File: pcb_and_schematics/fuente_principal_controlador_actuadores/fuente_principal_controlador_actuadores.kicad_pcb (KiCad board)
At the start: 2 copper layers, 166.1 x 108.2 mm, 78 parts, among them J1 Screw_Terminal_01x02, J10 Screw_Terminal_01x02, J11 Conn_01x15_Female, J12 Conn_01x15_Female, J2 Screw_Terminal_01x02, J3 Screw_Terminal_01x02, J4 Screw_Terminal_01x02, J5 Screw_Terminal_01x02, J6 Screw_Terminal_01x02, J7 Screw_Terminal_01x02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

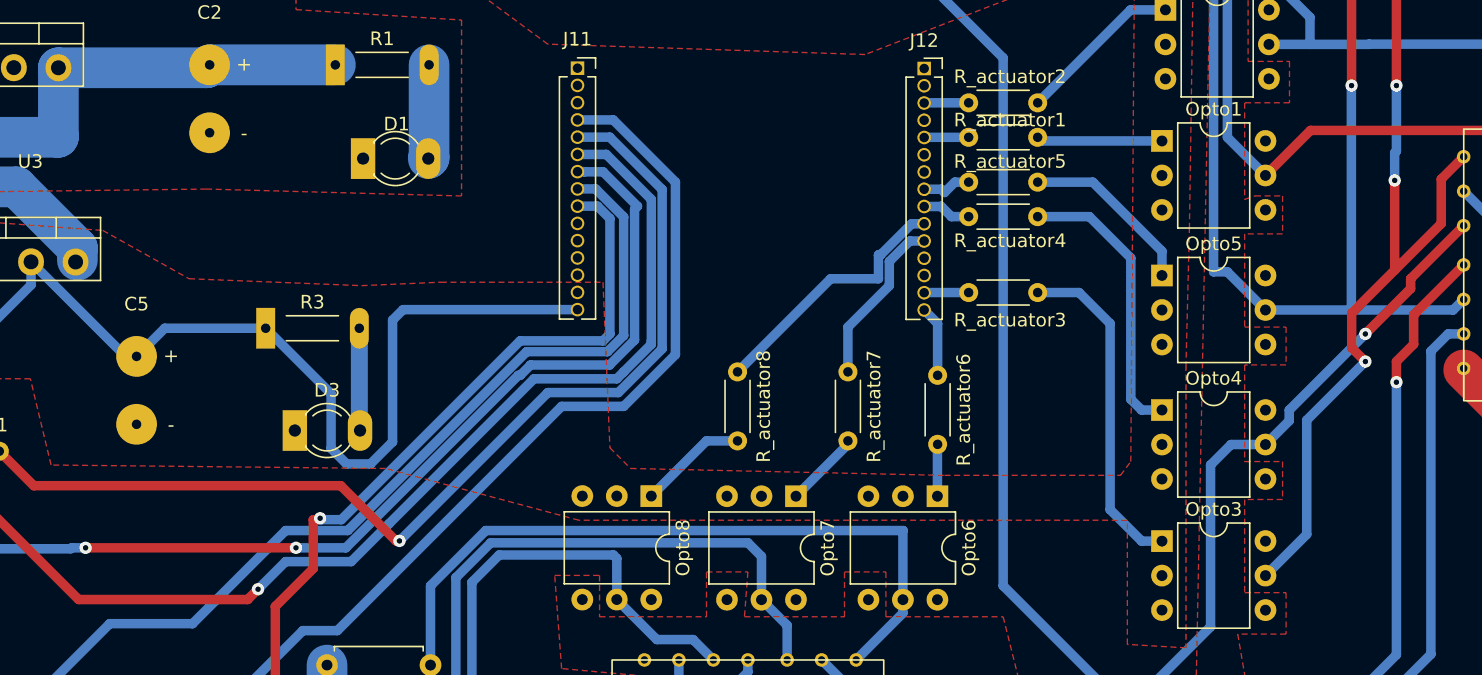
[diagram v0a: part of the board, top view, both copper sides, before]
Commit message: updated size of vias true holes, to make them bigger
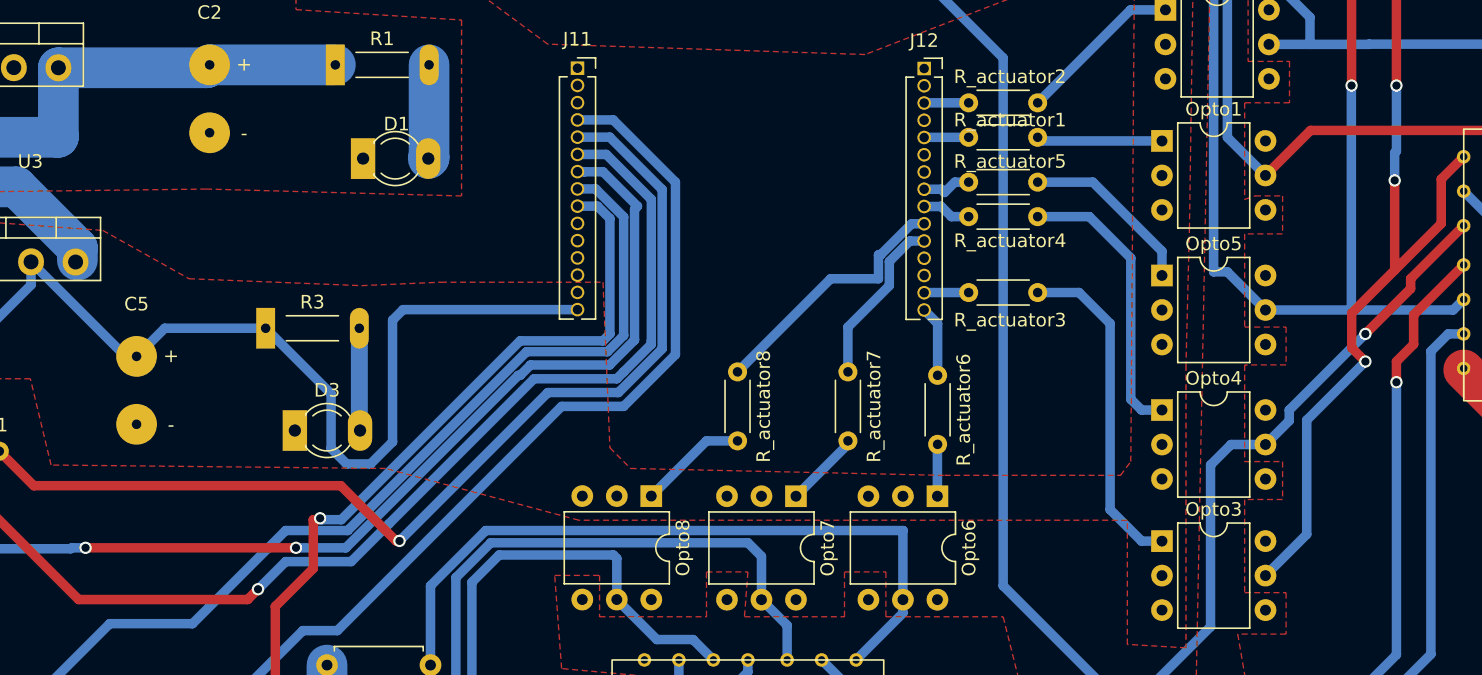
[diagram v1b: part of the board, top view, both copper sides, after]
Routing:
- net GND 3.3V: track 0.65 -> 0.00 mm
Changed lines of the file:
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@@
     (pts (xy 202.438 25.4) (xy 202.692 133.604))
     (height -7.844)
-    (gr_text "108,2043 mm" (at 212.208973 79.479362 270.1344969) (layer "F.Cu")
+    (gr_text "108.2043 mm" (at 212.208973 79.479362 270.1344969) (layer "F.Cu")
       (effects (font (size 1.5 1.5) (thickness 0.3)))
     )
@@
     (pts (xy 35.306 134.874) (xy 200.406 134.874))
     (height 4.040198)
-    (gr_text "165,1000 mm" (at 123.698 142.24) (layer "F.Cu")
+    (gr_text "165.1000 mm" (at 123.698 142.24) (layer "F.Cu")
       (effects (font (size 1.5 1.5) (thickness 0.3)))
     )
@@
   (segment (start 57.595 64.932) (end 62.489 60.038) (width 3) (layer "B.Cu") (net 2))
   (segment (start 62.489 60.038) (end 69.067098 60.038) (width 3) (layer "B.Cu") (net 2))
-  (segment (start 78.382 77.978) (end 77.924 77.52) (width 0.7) (layer "B.Cu") (net 3))
   (segment (start 92.245674 75.265674) (end 92.245674 79.291674) (width 0.7) (layer "B.Cu") (net 4))
   (segment (start 79.996 70.448) (end 77.924 72.52) (width 0.7) (layer "B.Cu") (net 4))
@@
   (segment (start 73.66 90.424) (end 62.738 79.502) (width 0.7) (layer "F.Cu") (net 19))
   (segment (start 86.106 90.424) (end 73.66 90.424) (width 0.7) (layer "F.Cu") (net 19))
-  (via (at 86.868 89.662) (size 0.91) (drill 0.4) (layers "F.Cu" "B.Cu") (net 19))
+  (via (at 86.868 89.662) (size 0.91) (drill 0.6) (layers "F.Cu" "B.Cu") (net 19))
   (segment (start 93.726 87.63) (end 88.9 87.63) (width 0.7) (layer "B.Cu") (net 19))
   (segment (start 110.39 57.648) (end 112.512 57.648) (width 0.7) (layer "B.Cu") (net 19))
@@
   (segment (start 112.512 57.648) (end 115.824 60.96) (width 0.7) (layer "B.Cu") (net 19))
   (segment (start 89.662 86.614) (end 74.168 86.614) (width 0.7) (layer "F.Cu") (net 20))
-  (via (at 89.662 86.614) (size 0.91) (drill 0.4) (layers "F.Cu" "B.Cu") (free) (net 20))
-  (via (at 74.168 86.614) (size 0.91) (drill 0.4) (layers "F.Cu" "B.Cu") (net 20))
+  (via (at 89.662 86.614) (size 0.91) (drill 0.6) (layers "F.Cu" "B.Cu") (free) (net 20))
+  (via (at 74.168 86.614) (size 0.91) (drill 0.6) (layers "F.Cu" "B.Cu") (net 20))
   (segment (start 114.592 61.684) (end 114.592 71.31274) (width 0.7) (layer "B.Cu") (net 20))
   (segment (start 106.172 73.914) (end 106.03337 73.914) (width 0.7) (layer "B.Cu") (net 20))
-  (segment (start 73.08312 86.68288) (end 58.892249 86.68288) (width 0.7) (layer "B.Cu") (net 20))
-  (segment (start 73.152 86.614) (end 73.08312 86.68288) (width 0.7) (layer "B.Cu") (net 20))
+  (segment (start 74.168 86.614) (end 73.152 86.614) (width 0.7) (layer "B.Cu") (net 20))
   (segment (start 114.808 61.468) (end 114.592 61.684) (width 0.7) (layer "B.Cu") (net 20))
   (segment (start 112.268 58.928) (end 114.808 61.468) (width 0.7) (layer "B.Cu") (net 20))
   (segment (start 106.03337 73.914) (end 93.33337 86.614) (width 0.7) (layer "B.Cu") (net 20))
   (segment (start 93.33337 86.614) (end 89.662 86.614) (width 0.7) (layer "B.Cu") (net 20))
-  (segment (start 74.168 86.614) (end 73.152 86.614) (width 0.7) (layer "B.Cu") (net 20))
   (segment (start 106.934 73.152) (end 106.172 73.914) (width 0.7) (layer "B.Cu") (net 20))
   (segment (start 114.592 71.31274) (end 112.75274 73.152) (width 0.7) (layer "B.Cu") (net 20))
   (segment (start 110.39 58.918) (end 110.910001 58.918) (width 0.7) (layer "B.Cu") (net 20))
+  (segment (start 73.08312 86.68288) (end 58.892249 86.68288) (width 0.7) (layer "B.Cu") (net 20))
+  (segment (start 73.152 86.614) (end 73.08312 86.68288) (width 0.7) (layer "B.Cu") (net 20))
   (segment (start 112.75274 73.152) (end 106.934 73.152) (width 0.7) (layer "B.Cu") (net 20))
   (segment (start 110.910001 58.918) (end 110.920001 58.928) (width 0.7) (layer "B.Cu") (net 20))
   (segment (start 110.920001 58.928) (end 112.268 58.928) (width 0.7) (layer "B.Cu") (net 20))
   (segment (start 70.358 82.042) (end 67.818 79.502) (width 0.7) (layer "F.Cu") (net 21))
+  (segment (start 92.964 82.042) (end 70.358 82.042) (width 0.7) (layer "F.Cu") (net 21))
   (segment (start 97.028 86.106) (end 92.964 82.042) (width 0.7) (layer "F.Cu") (net 21))
-  (segment (start 92.964 82.042) (end 70.358 82.042) (width 0.7) (layer "F.Cu") (net 21))
   (segment (start 97.282 86.106) (end 97.028 86.106) (width 0.7) (layer "F.Cu") (net 21))
-  (via (at 97.282 86.106) (size 0.91) (drill 0.4) (layers "F.Cu" "B.Cu") (free) (net 21))
+  (via (at 97.282 86.106) (size 0.91) (drill 0.6) (layers "F.Cu" "B.Cu") (free) (net 21))
+  (segment (start 97.282 86.106) (end 97.286579 86.106) (width 0.7) (layer "B.Cu") (net 21))
   (segment (start 56.896 83.318001) (end 56.896 81.679129) (width 0.7) (layer "B.Cu") (net 21))
+  (segment (start 116.624 60.236) (end 112.766 56.378) (width 0.7) (layer "B.Cu") (net 21))
   (segment (start 58.892249 84.18288) (end 57.760879 84.18288) (width 0.7) (layer "B.Cu") (net 21))
   (segment (start 56.896 81.679129) (end 58.892249 79.68288) (width 0.7) (layer "B.Cu") (net 21))
   (segment (start 112.766 56.378) (end 110.39 56.378) (width 0.7) (layer "B.Cu") (net 21))
-  (segment (start 116.624 60.236) (end 112.766 56.378) (width 0.7) (layer "B.Cu") (net 21))
-  (segment (start 97.286579 86.106) (end 108.208579 75.184) (width 0.7) (layer "B.Cu") (net 21))
+  (segment (start 108.208579 75.184) (end 113.39937 75.184) (width 0.7) (layer "B.Cu") (net 21))
   (segment (start 116.624 71.95937) (end 116.624 60.236) (width 0.7) (layer "B.Cu") (net 21))
   (segment (start 57.760879 84.18288) (end 56.896 83.318001) (width 0.7) (layer "B.Cu") (net 21))
-  (segment (start 97.282 86.106) (end 97.286579 86.106) (width 0.7) (layer "B.Cu") (net 21))
-  (segment (start 113.39937 75.184) (end 116.624 71.95937) (width 0.7) (layer "B.Cu") (net 21))
+  (segment (start 97.286579 86.106) (end 108.208579 75.184) (width 0.7) (layer "B.Cu") (net 21))
   (segment (start 59.861369 80.652) (end 58.892249 79.68288) (width 0.7) (layer "B.Cu") (net 21))
   (segment (start 67.818 79.502) (end 66.668 80.652) (width 0.7) (layer "B.Cu") (net 21))
-  (segment (start 108.208579 75.184) (end 113.39937 75.184) (width 0.7) (layer "B.Cu") (net 21))
   (segment (start 66.668 80.652) (end 59.861369 80.652) (width 0.7) (layer "B.Cu") (net 21))
+  (segment (start 113.39937 75.184) (end 116.624 71.95937) (width 0.7) (layer "B.Cu") (net 21))
   (segment (start 59.682874 120.888) (end 59.208 120.888) (width 0.7) (layer "B.Cu") (net 22))
   (segment (start 77.978 102.592874) (end 59.682874 120.888) (width 0.7) (layer "B.Cu") (net 22))
@@
   (segment (start 91.3355 84.544) (end 90.932 84.544) (width 0.7) (layer "F.Cu") (net 37))
   (segment (start 80.248 105.172) (end 80.248 116.078) (width 0.7) (layer "F.Cu") (net 37))
-  (via (at 91.44 84.4395) (size 0.91) (drill 0.4) (layers "F.Cu" "B.Cu") (free) (net 37))
+  (via (at 91.44 84.4395) (size 0.91) (drill 0.6) (layers "F.Cu" "B.Cu") (free) (net 37))
   (segment (start 106.172 71.374) (end 93.002 84.544) (width 0.7) (layer "B.Cu") (net 37))
   (segment (start 93.002 84.544) (end 91.5445 84.544) (width 0.7) (layer "B.Cu") (net 37))
@@
   (segment (start 173.99 59.4675) (end 173.99 62.738) (width 0.7) (layer "F.Cu") (net 62))
   (segment (start 167.397 69.331) (end 167.397 71.893) (width 0.7) (layer "F.Cu") (net 62))
-  (via (at 170.561 59.563) (size 0.91) (drill 0.4) (layers "F.Cu" "B.Cu") (net 62))
-  (via (at 170.688 52.578) (size 0.91) (drill 0.4) (layers "F.Cu" "B.Cu") (net 62))
-  (via (at 168.402 72.898) (size 0.91) (drill 0.4) (layers "F.Cu" "B.Cu") (free) (net 62))
+  (via (at 170.561 59.563) (size 0.91) (drill 0.6) (layers "F.Cu" "B.Cu") (net 62))
+  (via (at 170.688 52.578) (size 0.91) (drill 0.6) (layers "F.Cu" "B.Cu") (net 62))
+  (via (at 168.402 72.898) (size 0.91) (drill 0.6) (layers "F.Cu" "B.Cu") (free) (net 62))
   (segment (start 164.084 77.216) (end 168.402 72.898) (width 0.7) (layer "B.Cu") (net 62))
   (segment (start 170.688 57.404) (end 170.688 52.578) (width 0.7) (layer "B.Cu") (net 62))
@@
   (segment (start 171.7355 66.802) (end 171.7355 67.5325) (width 0.7) (layer "F.Cu") (net 66))
   (segment (start 175.641 62.8965) (end 171.7355 66.802) (width 0.7) (layer "F.Cu") (net 66))
-  (via (at 168.402 70.866) (size 0.91) (drill 0.4) (layers "F.Cu" "B.Cu") (free) (net 66))
+  (via (at 168.402 70.866) (size 0.91) (drill 0.6) (layers "F.Cu" "B.Cu") (free) (net 66))
   (segment (start 137.044 45.858) (end 119.264 45.858) (width 0.7) (layer "B.Cu") (net 66))
   (segment (start 119.264 45.858) (end 116.586 43.18) (width 0.7) (layer "B.Cu") (net 66))
@@
   (segment (start 167.386 52.578) (end 167.386 42.672) (width 0.7) (layer "F.Cu") (net 70))
   (segment (start 160.274 35.56) (end 120.904 35.56) (width 0.7) (layer "F.Cu") (net 70))
-  (via (at 167.386 52.578) (size 0.91) (drill 0.4) (layers "F.Cu" "B.Cu") (net 70))
+  (via (at 167.386 52.578) (size 0.91) (drill 0.6) (layers "F.Cu" "B.Cu") (net 70))
   (segment (start 158.237 66.294) (end 161.046 69.103) (width 0.7) (layer "B.Cu") (net 70))
   (segment (start 157.226 66.294) (end 158.237 66.294) (width 0.7) (layer "B.Cu") (net 70))
@@
   (segment (start 171.958 69.469) (end 175.641 65.786) (width 0.7) (layer "F.Cu") (net 95))
   (segment (start 171.958 71.628) (end 171.958 69.469) (width 0.7) (layer "F.Cu") (net 95))
-  (via (at 170.688 74.422) (size 0.91) (drill 0.4) (layers "F.Cu" "B.Cu") (free) (net 95))
+  (via (at 170.688 74.422) (size 0.91) (drill 0.6) (layers "F.Cu" "B.Cu") (free) (net 95))
   (segment (start 165.1 100.076) (end 157.988 100.076) (width 0.7) (layer "B.Cu") (net 95))
   (segment (start 152.146 105.918) (end 150.836 105.918) (width 0.7) (layer "B.Cu") (net 95))

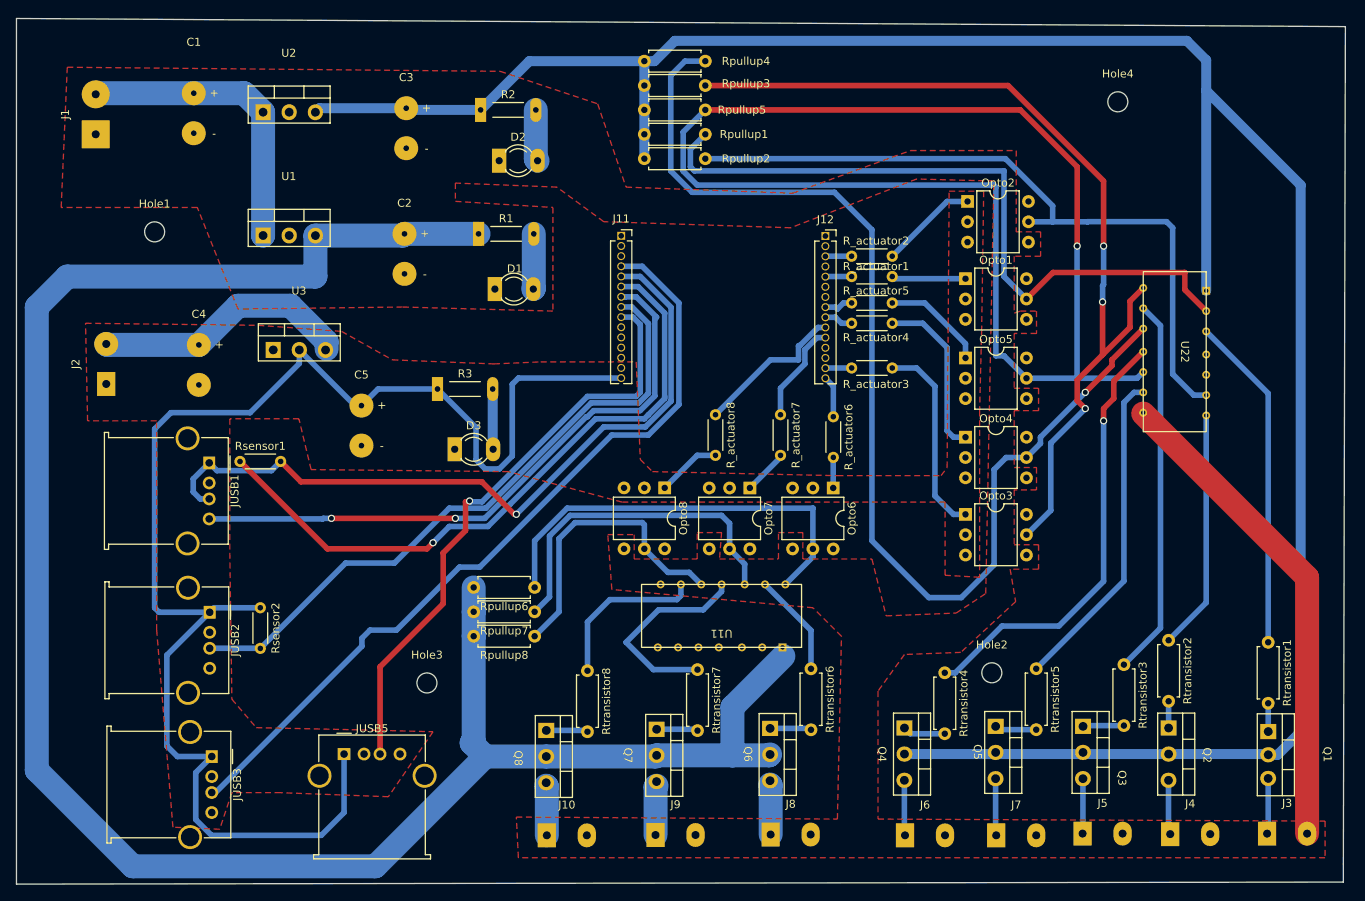
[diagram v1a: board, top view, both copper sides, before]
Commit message: corrections in order to adapt to manufacturer constraints, and correction of size and spacing on esp32 pins
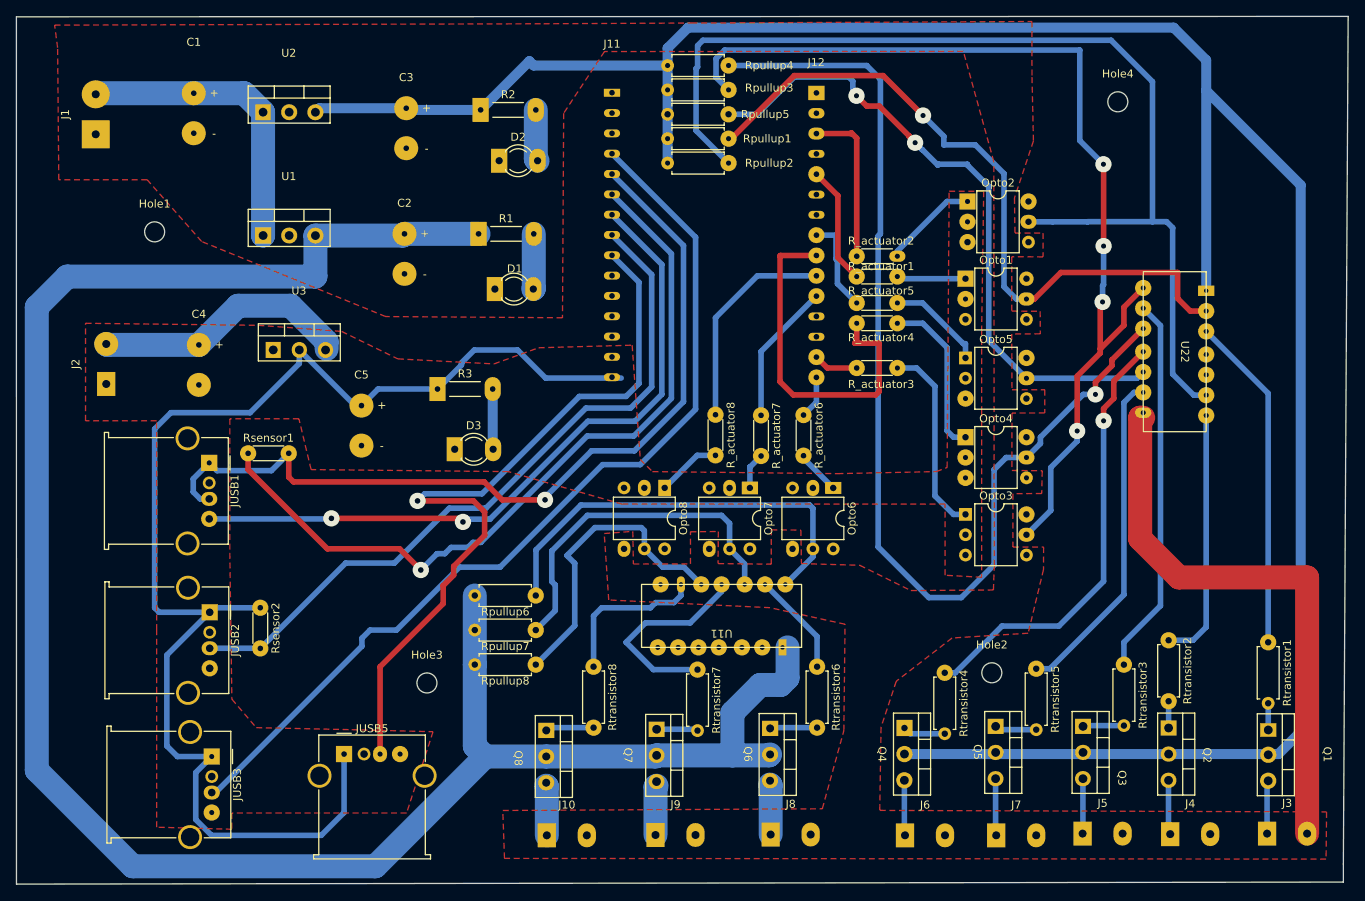
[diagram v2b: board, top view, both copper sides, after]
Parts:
- moved R_actuator6 3.73 mm to (133.2, 73.7)
- moved Rpullup8 3.55 mm to (99.7, 104.9)
- moved Rpullup1 2.96 mm to (123.8, 39.2)
- moved Rpullup4 2.96 mm to (123.8, 30.0)
- moved Rpullup2 2.96 mm to (123.8, 42.2)
- moved Rpullup3 2.96 mm to (123.8, 33.1)
- moved Rpullup5 2.96 mm to (123.8, 36.1)
- moved R_actuator7 2.43 mm to (127.9, 73.7)
- moved Rpullup7 2.28 mm to (99.7, 100.6)
- moved Rsensor1 1.44 mm to (63.8, 78.5)
- moved J11 1.16 mm to (109.2, 51.2)
- moved J12 1.16 mm to (134.8, 51.2)
- moved Rpullup6 1.02 mm to (99.7, 96.3)
- moved Rtransistor8 0.92 mm to (106.9, 105.2)
- moved Rtransistor6 0.81 mm to (134.9, 105.2)
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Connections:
- J12 pad 4: unconnected-(J12-Pad4) -> (no net)
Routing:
- net Net-(Opto5-Pad5): track 165.6 -> 82.0 mm, vias 1 -> 2
- net Net-(Opto2-Pad5): track 89.8 -> 135.1 mm
- net pump4: track 3.60 -> 45.2 mm
- net Signal ExtraSensor: track 74.7 -> 95.8 mm
- net pump1: track 3.28 -> 20.1 mm
- net signal PH: track 100.9 -> 117.2 mm
- net signal EC: track 93.6 -> 109.0 mm
- net 3.3V ec: track 82.9 -> 97.6 mm
- net 3.3VDC: track 181.7 -> 168.5 mm
- net Net-(Opto3-Pad5): track 114.2 -> 126.1 mm, vias 3 -> 4
- net pump2: track 3.28 -> 14.9 mm
- net GND ec: track 77.5 -> 88.4 mm
- net GND pot: track 61.0 -> 70.4 mm
- net signal DB18B20: track 81.0 -> 89.8 mm
- net pump3: track 3.69 -> 12.0 mm
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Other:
- board size 166.1 x 108.2 mm -> 166.5 x 108.5 mm
